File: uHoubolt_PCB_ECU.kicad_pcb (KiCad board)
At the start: 4 copper layers, 118 parts, among them J1 Power In, J10 Servo 1, J11 PYRO 1, J2 Conn_02x04_Odd_Even, J3 CAN1, J4 CAN2, J5 CAN1, J6 CAN2, J7 Pressure 1, J8 TEMP 1, J9 OUT 1, Q1 SISA88DN or similar, U1 SiC431CED-T1-GE3, U10 INA180A1, U11 INA180A1, U2 TS30041-M050QFNR, U3 MCP1700-3302E, U4 MCP2562FDT-H_SN, U5 MCP2562FDT-H_SN, U6 STM32G491MET6-LQFP80, U7 ICM-20602, U8 W25Q256JV, U9 TPS1HC100, X1 TXC-7C

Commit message: schematic even more done
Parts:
- removed C24: 100n, Capacitor_SMD:C_0402_1005Metric
- added JP2: VDD, Jumper:SolderJumper-2_P1.3mm_Bridged_RoundedPad1.0x1.5mm, F.Cu at (86.0, 124.0)
- added JP3: VDRV, Jumper:SolderJumper-2_P1.3mm_Bridged_RoundedPad1.0x1.5mm, F.Cu at (90.3, 124.0)
- C10: value 10µ -> 100µ; footprint Capacitor_SMD:C_0603_1608Metric -> Capacitor_SMD:C_1210_3225Metric
- C25: value 10n -> 100n
- C28, C29: value 1u -> 2µ2
- C3: value 4µ7 -> 22µ
- C30: value 1u -> 100n; footprint Capacitor_SMD:C_0603_1608Metric -> Capacitor_SMD:C_0402_1005Metric
- C4: value 1µ -> 2µ2
- J1: footprint Connector_Molex:Molex_Mega-Fit_76825-0004_2x02_P5.70mm_Horizontal -> TXV_LIB:Molex_MegaFit_1x03
- J11: footprint Connector_Molex:Molex_SL_171971-0002_1x02_P2.54mm_Vertical -> TXV_LIB:Molex_SL_1x2
- J2: value Conn_02x04_Odd_Even -> Debug
- LS1: value Speaker_Crystal -> Speaker
- R10: value 115k -> 100k
- R11, R14, R16, R24, R27, R34, R4, R8: value 10k -> 9k1
- R12: value 6.8k -> 22k
- R13: value 4.7k -> 9k1
- R15: value 2k -> 9k1
- R19, R20, R21, R23: value LED -> 120
- R28: value 1k -> 120
- R3, R6: value LED -> 1k
- R33, R36: value 10k -> 22k
- R5, R9: value 2k -> 1k
- U1: value SiC431CED-T1-GE3 -> SiC431C
- U10, U11: value INA180A1 -> INA180B1; footprint Package_TO_SOT_SMD:SOT-23-6 -> Package_TO_SOT_SMD:SOT-23-5
- U5: value MCP2562FDT-H_SN -> MCP2562FDT
- moved R12 89.6 mm to (85.0, 92.0)
- moved R13 77.7 mm to (86.0, 95.0)
- moved C21 25.6 mm to (166.5, 121.2)
- moved C22 25.6 mm to (165.4, 123.4)
- moved C26 25.6 mm to (166.7, 118.2)
- moved C27 25.6 mm to (167.9, 124.5)
- moved R17 25.6 mm to (170.1, 121.0)
- moved R18 25.6 mm to (172.2, 124.2)
- moved J6 21.5 mm to (154.7, 113.5)
- moved C30 16.5 mm to (144.0, 38.0)
- moved U5 14.2 mm to (154.7, 125.3), turned to 90 degrees
- moved U4 14.1 mm to (145.3, 125.3), turned to 90 degrees
- moved J1 13.4 mm to (67.5, 61.0), turned to 90 degrees
- moved R22 13.0 mm to (207.7, 90.5)
- moved J3 12.6 mm to (145.3, 119.9)
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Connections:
- net /Buzzer_N renamed /Speaker_N
- net /Buzzer_P renamed /Speaker_P
- C1 pad 1: Net-(C1-Pad1) -> +12V
- C2 pad 1: Net-(C1-Pad1) -> +12V
- C5 pad 1: Net-(C1-Pad1) -> +12V
- C6 pad 1: Net-(C1-Pad1) -> +12V
- C7 pad 1: Net-(C1-Pad1) -> +12V
- J8 pad MP: (no net) -> GND
- U1 pad 1: Net-(C1-Pad1) -> +12V
- U1 pad 2: Net-(C1-Pad1) -> +12V
- U1 pad 22: Net-(C1-Pad1) -> +12V
- U1 pad 26: Net-(C1-Pad1) -> +12V
- U10 pad 1: Net-(R25-Pad2) -> Net-(J7-Pad2)
- U10 pad 3: Net-(J7-Pad2) -> Net-(J7-Pad3)
- U10 pad 4: Net-(J7-Pad3) -> Net-(R25-Pad2)
- U10 pad 5: (no net) -> +3V3
- U11 pad 1: /SERVO_1_CURR -> +7.4V
- U11 pad 3: +7.4V -> Net-(J10-Pad3)
- U11 pad 4: Net-(J10-Pad3) -> /SERVO_1_CURR
- U11 pad 5: (no net) -> +3V3
- U5 pad 9: (no net) -> GND
- U6 pad 59: Net-(U6-Pad59) -> /CAN1_RX
- U6 pad 60: Net-(U6-Pad60) -> /CAN1_TX
- U6 pad 65: Net-(U6-Pad65) -> /SPI_IMU_CS
- U6 pad 66: Net-(U6-Pad66) -> /SPI_SCK
- U6 pad 67: Net-(U6-Pad67) -> /SPI_MISO
- U6 pad 68: Net-(U6-Pad68) -> /SPI_MOSI
- U6 pad 69: Net-(U6-Pad69) -> /IMU_INT
- U6 pad 74: Net-(U6-Pad74) -> /CAN2_RX
- U6 pad 75: Net-(U6-Pad75) -> /CAN2_TX
- U7 pad 2: /SPI_CLK -> /SPI_SCK
- U7 pad 6: /IMU_INTERRUPT -> /IMU_INT
- U9 pad 8: Net-(U9-Pad8) -> Net-(J11-Pad1)
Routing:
- net /PRESS_1: track 4.20 -> 1.43 mm
- net Net-(R25-Pad2): track 2.90 -> 4.88 mm
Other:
- board outline added: 65 x 62 mm

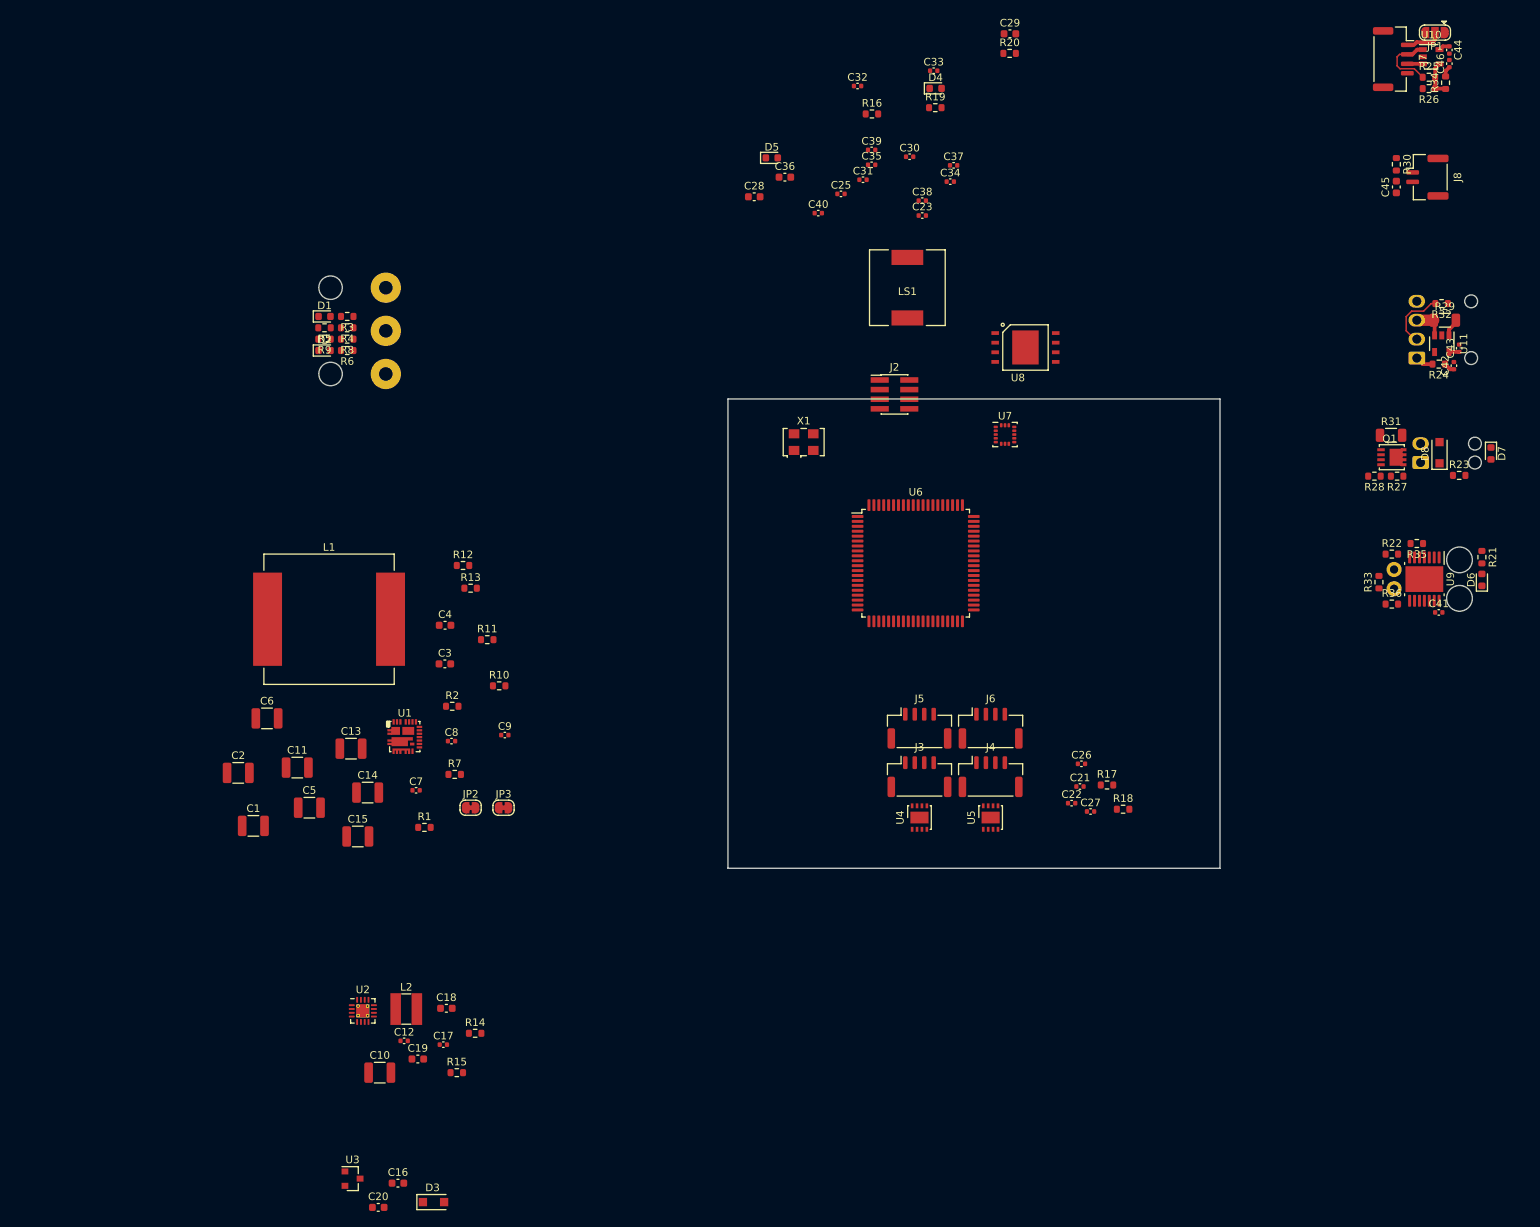
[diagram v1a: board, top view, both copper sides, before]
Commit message: moved I/O to subsheets, started layout
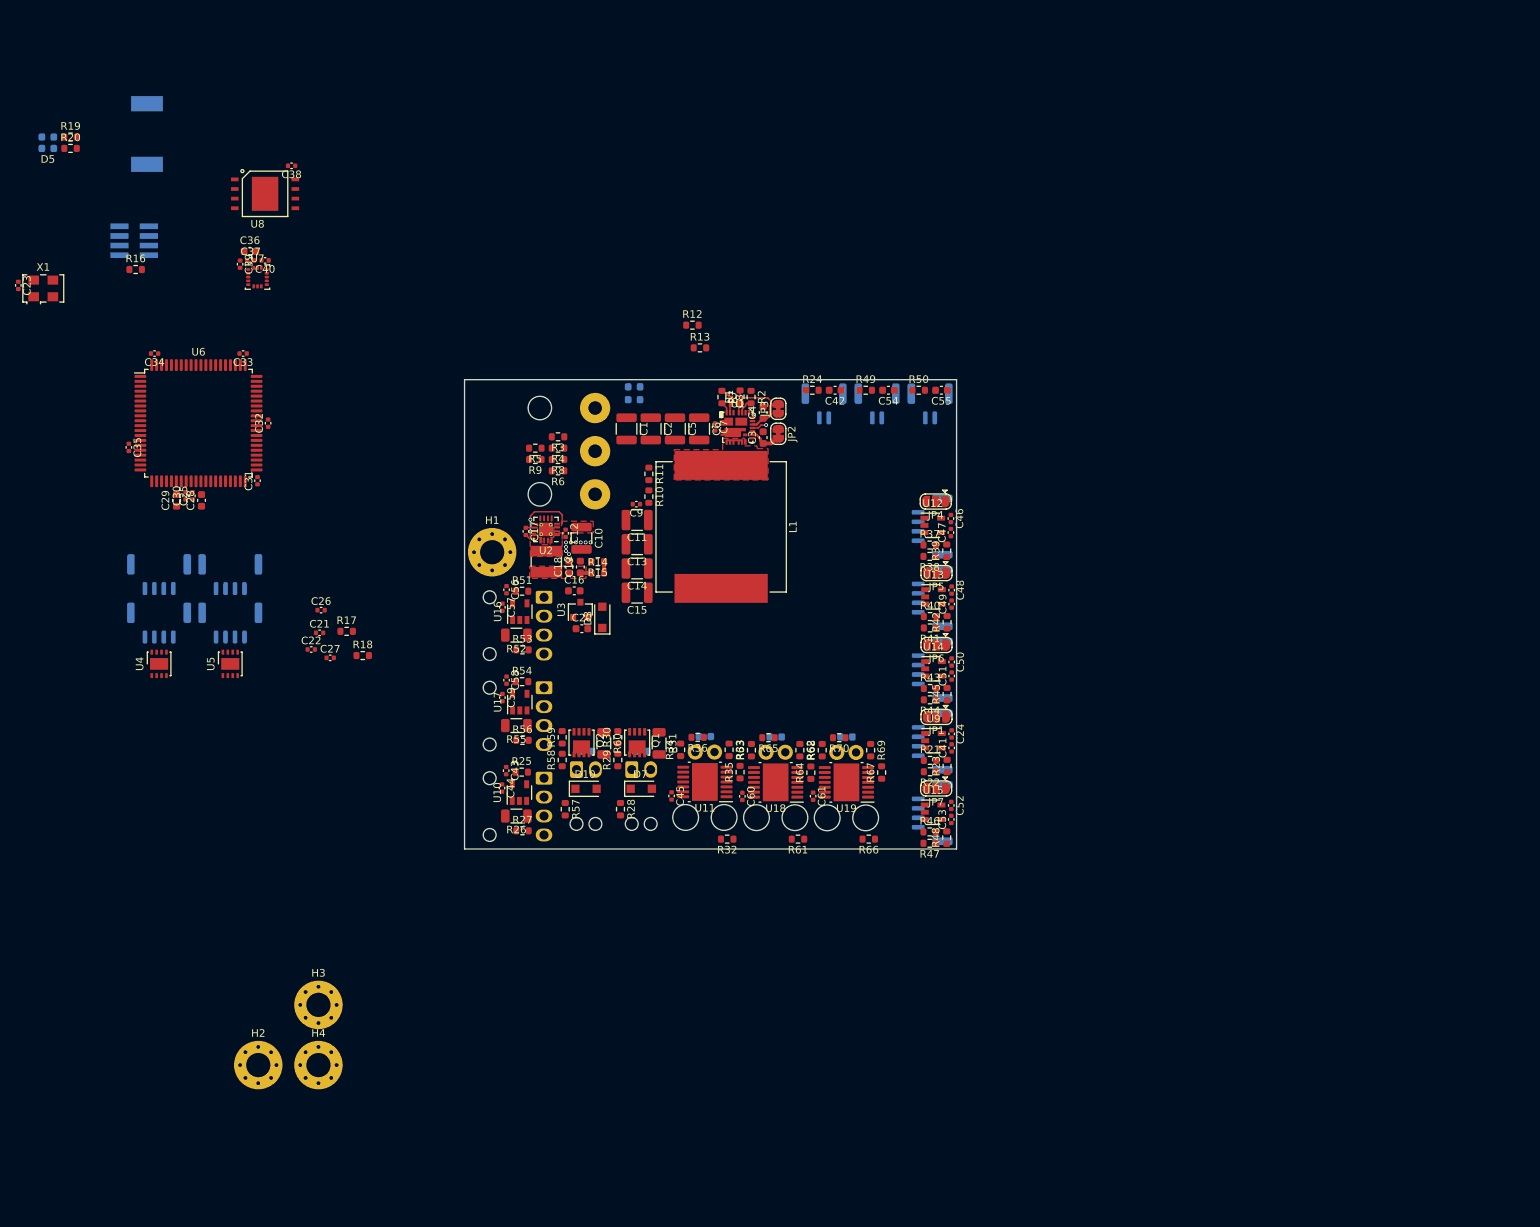
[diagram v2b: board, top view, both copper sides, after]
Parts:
- added C24: 100n, Capacitor_SMD:C_0402_1005Metric, F.Cu at (149.6, 114.2)
- added C47: 100n, Capacitor_SMD:C_0402_1005Metric, F.Cu at (149.4, 87.7)
- added C48: 100n, Capacitor_SMD:C_0402_1005Metric, F.Cu at (149.6, 95.2)
- added C49: 100n, Capacitor_SMD:C_0402_1005Metric, F.Cu at (149.6, 97.1)
- added C50: 100n, Capacitor_SMD:C_0402_1005Metric, F.Cu at (149.6, 104.8)
- added C51: 100n, Capacitor_SMD:C_0402_1005Metric, F.Cu at (149.6, 106.6)
- added C52: 100n, Capacitor_SMD:C_0402_1005Metric, F.Cu at (149.5, 123.7)
- added C53: 100n, Capacitor_SMD:C_0402_1005Metric, F.Cu at (149.5, 125.5)
- added C54: 22µ, Capacitor_SMD:C_0603_1608Metric, F.Cu at (141.2, 68.8)
- added C55: 22µ, Capacitor_SMD:C_0603_1608Metric, F.Cu at (148.2, 68.8)
- added C56: 100n, Capacitor_SMD:C_0402_1005Metric, F.Cu at (90.8, 95.2)
- added C57: 100n, Capacitor_SMD:C_0402_1005Metric, F.Cu at (90.2, 97.5)
- added C58: 100n, Capacitor_SMD:C_0402_1005Metric, F.Cu at (90.8, 107.2)
- added C59: 100n, Capacitor_SMD:C_0402_1005Metric, F.Cu at (90.2, 109.5)
- added C60: 100n, Capacitor_SMD:C_0402_1005Metric, F.Cu at (121.9, 122.5)
- added C61: 100n, Capacitor_SMD:C_0402_1005Metric, F.Cu at (131.2, 122.5)
- added D10: Shottky, Diode_SMD:D_SOD-123F, F.Cu at (101.2, 121.5)
- added D11: PYRO 1, LED_SMD:LED_0603_1608Metric, B.Cu at (126.3, 114.7)
- added D12: PYRO 1, LED_SMD:LED_0603_1608Metric, B.Cu at (135.7, 114.7)
- added D9: OUT 1, LED_SMD:LED_0603_1608Metric, B.Cu at (101.2, 116.5)
- added H1: MH, MountingHole:MountingHole_3.2mm_M3_Pad_Via, F.Cu at (88.8, 90.2)
- added H2: MH, MountingHole:MountingHole_3.2mm_M3_Pad_Via, F.Cu at (58.0, 158.0)
- added H3: MH, MountingHole:MountingHole_3.2mm_M3_Pad_Via, F.Cu at (65.9, 150.1)
- added H4: MH, MountingHole:MountingHole_3.2mm_M3_Pad_Via, F.Cu at (65.9, 158.0)
- added J12: Pressure 1, Connector_JST:JST_GH_SM04B-GHS-TB_1x04-1MP_P1.25mm_Horizontal, B.Cu at (147.0, 86.9)
- added J13: Pressure 1, Connector_JST:JST_GH_SM04B-GHS-TB_1x04-1MP_P1.25mm_Horizontal, B.Cu at (147.0, 96.3)
- added J14: Pressure 1, Connector_JST:JST_GH_SM04B-GHS-TB_1x04-1MP_P1.25mm_Horizontal, B.Cu at (147.0, 105.8)
- added J15: Pressure 1, Connector_JST:JST_GH_SM04B-GHS-TB_1x04-1MP_P1.25mm_Horizontal, B.Cu at (147.0, 124.7)
- added J16: TEMP 1, Connector_JST:JST_GH_SM02B-GHS-TB_1x02-1MP_P1.25mm_Horizontal, B.Cu at (139.7, 70.7)
- added J17: TEMP 1, Connector_JST:JST_GH_SM02B-GHS-TB_1x02-1MP_P1.25mm_Horizontal, B.Cu at (146.7, 70.7)
- added J18: Servo 1, Connector_Molex:Molex_Nano-Fit_105313-xx04_1x04_P2.50mm_Horizontal, B.Cu at (95.7, 96.2)
- added J19: Servo 1, Connector_Molex:Molex_Nano-Fit_105313-xx04_1x04_P2.50mm_Horizontal, B.Cu at (95.7, 108.2)
- added J20: OUT 1, Connector_Molex:Molex_Nano-Fit_105313-xx02_1x02_P2.50mm_Horizontal, B.Cu at (100.0, 119.0)
- added J21: PYRO 1, TXV_LIB:Molex_SL_1x2, B.Cu at (126.3, 116.7)
- added J22: PYRO 1, TXV_LIB:Molex_SL_1x2, B.Cu at (135.7, 116.7)
- added JP4: V_SEL, Jumper:SolderJumper-3_P1.3mm_Open_RoundedPad1.0x1.5mm, F.Cu at (147.4, 83.5)
- added JP5: V_SEL, Jumper:SolderJumper-3_P1.3mm_Open_RoundedPad1.0x1.5mm, F.Cu at (147.6, 93.0)
- added JP6: V_SEL, Jumper:SolderJumper-3_P1.3mm_Open_RoundedPad1.0x1.5mm, F.Cu at (147.6, 102.5)
- added JP7: V_SEL, Jumper:SolderJumper-3_P1.3mm_Open_RoundedPad1.0x1.5mm, F.Cu at (147.5, 121.5)
- added Q2: SISA88DN or similar, TXV_LIB:PowerPAK_1212-8, F.Cu at (100.7, 115.1)
- added R37: 4k7/0, Resistor_SMD:R_0603_1608Metric, F.Cu at (146.7, 89.3)
- added R38: 6k8/160, Resistor_SMD:R_0603_1608Metric, F.Cu at (146.7, 90.8)
- added R39: 9k1, Resistor_SMD:R_0603_1608Metric, F.Cu at (148.9, 90.0)
- added R40: 4k7/0, Resistor_SMD:R_0603_1608Metric, F.Cu at (146.7, 98.8)
- added R41: 6k8/160, Resistor_SMD:R_0603_1608Metric, F.Cu at (146.7, 100.2)
- added R42: 9k1, Resistor_SMD:R_0603_1608Metric, F.Cu at (148.9, 99.5)
- added R43: 4k7/0, Resistor_SMD:R_0603_1608Metric, F.Cu at (146.7, 108.2)
- added R44: 6k8/160, Resistor_SMD:R_0603_1608Metric, F.Cu at (146.7, 109.8)
- added R45: 9k1, Resistor_SMD:R_0603_1608Metric, F.Cu at (148.9, 109.0)
- added R46: 4k7/0, Resistor_SMD:R_0603_1608Metric, F.Cu at (146.7, 127.2)
- added R47: 6k8/160, Resistor_SMD:R_0603_1608Metric, F.Cu at (146.7, 128.7)
- added R48: 9k1, Resistor_SMD:R_0603_1608Metric, F.Cu at (148.9, 128.0)
- added R49: 1k, Resistor_SMD:R_0603_1608Metric, F.Cu at (138.2, 68.8)
- added R50: 1k, Resistor_SMD:R_0603_1608Metric, F.Cu at (145.2, 68.8)
- added R51: 9k1, Resistor_SMD:R_0603_1608Metric, F.Cu at (92.8, 95.4)
- added R52: 10m 1W, Resistor_SMD:R_1206_3216Metric, F.Cu at (92.0, 101.2)
- added R53: 1k, Resistor_SMD:R_0603_1608Metric, F.Cu at (92.8, 103.2)
- added R54: 9k1, Resistor_SMD:R_0603_1608Metric, F.Cu at (92.8, 107.3)
- added R55: 10m 1W, Resistor_SMD:R_1206_3216Metric, F.Cu at (92.0, 113.2)
- added R56: 1k, Resistor_SMD:R_0603_1608Metric, F.Cu at (92.8, 115.1)
- added R57: 120, Resistor_SMD:R_0603_1608Metric, F.Cu at (98.5, 124.2)
- added R58: 9k1, Resistor_SMD:R_0603_1608Metric, F.Cu at (98.1, 117.7)
- added R59: 120, Resistor_SMD:R_0603_1608Metric, F.Cu at (98.1, 114.7)
- added R60: 10m 1W, Resistor_SMD:R_1206_3216Metric, F.Cu at (103.6, 115.5)
- added R61: 120, Resistor_SMD:R_0603_1608Metric, F.Cu at (129.2, 128.2)
- added R62: 22k, Resistor_SMD:R_0603_1608Metric, F.Cu at (129.5, 116.4)
- added R63: 22k, Resistor_SMD:R_0603_1608Metric, F.Cu at (123.1, 116.4)
- added R64: 1k, Resistor_SMD:R_0603_1608Metric, F.Cu at (130.9, 119.4)
- added R65: 22k, Resistor_SMD:R_0603_1608Metric, F.Cu at (125.3, 114.8)
- added R66: 120, Resistor_SMD:R_0603_1608Metric, F.Cu at (138.6, 128.2)
- added R67: 22k, Resistor_SMD:R_0603_1608Metric, F.Cu at (140.3, 119.3)
- added R68: 22k, Resistor_SMD:R_0603_1608Metric, F.Cu at (132.4, 116.4)
- added R69: 1k, Resistor_SMD:R_0603_1608Metric, F.Cu at (138.8, 116.4)
- added R70: 22k, Resistor_SMD:R_0603_1608Metric, F.Cu at (134.7, 114.8)
- added U12: INA180B1, Package_TO_SOT_SMD:SOT-23-5, F.Cu at (147.1, 86.7)
- added U13: INA180B1, Package_TO_SOT_SMD:SOT-23-5, F.Cu at (147.2, 96.2)
- added U14: INA180B1, Package_TO_SOT_SMD:SOT-23-5, F.Cu at (147.2, 105.7)
- added U15: INA180B1, Package_TO_SOT_SMD:SOT-23-5, F.Cu at (147.1, 124.6)
- added U16: INA180B1, Package_TO_SOT_SMD:SOT-23-5, F.Cu at (92.5, 98.1)
- added U17: INA180B1, Package_TO_SOT_SMD:SOT-23-5, F.Cu at (92.5, 110.0)
- added U18: TPS1HC100, Package_SO:HTSSOP-14-1EP_4.4x5mm_P0.65mm_EP3.4x5mm_Mask3x3.1mm, F.Cu at (126.3, 120.7)
- added U19: TPS1HC100, Package_SO:HTSSOP-14-1EP_4.4x5mm_P0.65mm_EP3.4x5mm_Mask3x3.1mm, F.Cu at (135.7, 120.7)
- C42: value 100n -> 22µ; footprint Capacitor_SMD:C_0402_1005Metric -> Capacitor_SMD:C_0603_1608Metric
- C45: value 22µ -> 100n; footprint Capacitor_SMD:C_0603_1608Metric -> Capacitor_SMD:C_0402_1005Metric
- D1, D2, D4, D5, J2, J3, J4, J5, J6, J7, LS1: moved to B.Cu
- D6: value PYRO 1 -> OUT 1; moved to B.Cu
- D7: value OUT 1 -> Shottky; footprint LED_SMD:LED_0603_1608Metric -> Diode_SMD:D_SOD-123F
- D8: value Shottky -> PYRO 1; footprint Diode_SMD:D_SOD-123F -> LED_SMD:LED_0603_1608Metric; moved to B.Cu
- J10: value Servo 1 -> OUT 1; footprint Connector_Molex:Molex_Nano-Fit_105313-xx04_1x04_P2.50mm_Horizontal -> Connector_Molex:Molex_Nano-Fit_105313-xx02_1x02_P2.50mm_Horizontal
- J8: footprint Connector_JST:JST_GH_BM02B-GHS-TBT_1x02-1MP_P1.25mm_Vertical -> Connector_JST:JST_GH_SM02B-GHS-TB_1x02-1MP_P1.25mm_Horizontal; moved to B.Cu
- J9: value OUT 1 -> Servo 1; footprint Connector_Molex:Molex_Nano-Fit_105313-xx02_1x02_P2.50mm_Horizontal -> Connector_Molex:Molex_Nano-Fit_105313-xx04_1x04_P2.50mm_Horizontal
- R21: value 120 -> 4k7/0
- R22: value 22k -> 6k8/160
- R23: value 120 -> 9k1
- R24, R27: value 9k1 -> 1k
- R25: value 4k7/0 -> 9k1
- R26: value 6k8/160 -> 10m 1W; footprint Resistor_SMD:R_0603_1608Metric -> Resistor_SMD:R_1206_3216Metric
- R29: value 10m 1W -> 9k1; footprint Resistor_SMD:R_1206_3216Metric -> Resistor_SMD:R_0603_1608Metric
- R30, R32: value 1k -> 120
- R34: value 9k1 -> 22k
- U11: value INA180B1 -> TPS1HC100; footprint Package_TO_SOT_SMD:SOT-23-5 -> Package_SO:HTSSOP-14-1EP_4.4x5mm_P0.65mm_EP3.4x5mm_Mask3x3.1mm
- U9: value TPS1HC100 -> INA180B1; footprint Package_SO:HTSSOP-14-1EP_4.4x5mm_P0.65mm_EP3.4x5mm_Mask3x3.1mm -> Package_TO_SOT_SMD:SOT-23-5
- moved C44 158.6 mm to (90.2, 121.4)
- moved U10 154.8 mm to (92.5, 122.0), turned to 90 degrees
- moved R26 154.2 mm to (92.0, 125.1)
- moved R25 151.0 mm to (92.8, 119.3)
- moved C43 137.7 mm to (90.7, 119.1), turned to 270 degrees
- moved R34 134.1 mm to (113.8, 116.3)
- moved R30 127.7 mm to (105.5, 114.7), turned to 90 degrees
- moved C29 126.2 mm to (47.1, 83.4), turned to 90 degrees
- moved C45 125.1 mm to (112.5, 122.5), turned to 270 degrees
- moved R20 124.7 mm to (33.1, 36.9)
- moved R27 124.7 mm to (92.8, 127.0), turned to 0 degrees
- moved R29 123.7 mm to (105.5, 117.7), turned to 90 degrees
- moved J9 123.1 mm to (95.7, 120.1), turned to 180 degrees
- moved D7 120.7 mm to (108.5, 121.5), turned to 0 degrees
- moved C23 119.8 mm to (26.2, 55.0), turned to 270 degrees
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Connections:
- net /OUT_1_CURR renamed /OUT_2_CURR
- C41 pad 1: PYRO -> /PRESS_1
- C42 pad 1: /SERVO_1_FDBK -> GND
- C42 pad 2: GND -> /TEMP_1
- C43 pad 1: +3V3 -> /SERVO_1_FDBK
- C45 pad 1: GND -> PYRO
- C45 pad 2: /TEMP_1 -> GND
- C46 pad 1: /PRESS_1 -> +3V3
- D7 pad 1: GND -> +12V
- D8 pad 1: +12V -> GND
- J10 pad 1: Net-(J10-Pad1) -> +12V
- J10 pad 2: Net-(J10-Pad2) -> Net-(D7-Pad2)
- J9 pad 1: +12V -> Net-(J9-Pad1)
- J9 pad 2: Net-(D8-Pad2) -> Net-(J9-Pad2)
- Q1 pad 2: Net-(D8-Pad2) -> Net-(D7-Pad2)
- R21 pad 1: /PYRO_1_CTRL -> Net-(J7-Pad2)
- R21 pad 2: Net-(D6-Pad2) -> Net-(R21-Pad2)
- R22 pad 1: GND -> Net-(R21-Pad2)
- R22 pad 2: Net-(R22-Pad2) -> GND
- R23 pad 1: /OUT_1_CTRL -> Net-(R21-Pad2)
- R23 pad 2: Net-(D7-Pad2) -> /PRESS_1
- R24 pad 1: /SERVO_1_FDBK -> +3V3
- R24 pad 2: Net-(J10-Pad1) -> /TEMP_1
- R25 pad 1: Net-(J7-Pad2) -> /SERVO_1_FDBK
- R25 pad 2: Net-(R25-Pad2) -> Net-(J9-Pad1)
- R26 pad 1: Net-(R25-Pad2) -> Net-(J9-Pad3)
- R26 pad 2: GND -> +7.4V
- R27 pad 1: GND -> /SERVO_1_PWM
- R27 pad 2: /OUT_1_CTRL -> Net-(J9-Pad2)
- R28 pad 2: Net-(Q1-Pad1) -> Net-(D6-Pad2)
- R29 pad 1: Net-(J10-Pad3) -> GND
- R29 pad 2: +7.4V -> /OUT_1_CTRL
- R30 pad 1: +3V3 -> /OUT_1_CTRL
- R30 pad 2: /TEMP_1 -> Net-(Q1-Pad1)
- R32 pad 1: /SERVO_1_PWM -> /PYRO_1_CTRL
- R32 pad 2: Net-(J10-Pad2) -> Net-(D8-Pad2)
- R33 pad 1: Net-(J11-Pad1) -> GND
- R33 pad 2: +3V3 -> Net-(R33-Pad2)
- R34 pad 1: Net-(R25-Pad2) -> Net-(J11-Pad1)
- R34 pad 2: /PRESS_1 -> +3V3
- U10 pad 1: Net-(J7-Pad2) -> +7.4V
- U10 pad 3: Net-(J7-Pad3) -> Net-(J9-Pad3)
- U10 pad 4: Net-(R25-Pad2) -> /SERVO_1_CURR
- U11 pad 1: +7.4V -> GND
- U11 pad 2: GND -> /PYRO_1_CTRL
- U11 pad 3: Net-(J10-Pad3) -> +3V3
- U11 pad 4: /SERVO_1_CURR -> Net-(U11-Pad4)
- U11 pad 5: +3V3 -> GND
- U9 pad 1: GND -> Net-(J7-Pad2)
- U9 pad 2: /PYRO_1_CTRL -> GND
- U9 pad 3: +3V3 -> Net-(J7-Pad3)
- U9 pad 4: Net-(U9-Pad4) -> Net-(R21-Pad2)
- U9 pad 5: GND -> +3V3
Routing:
- net Net-(C4-Pad1): track 0.00 -> 10.8 mm
- net Net-(J7-Pad2): track 9.15 -> 0.00 mm
- net +12V: track 0.00 -> 8.45 mm, vias 0 -> 2
- net Net-(J10-Pad2): track 8.30 -> 0.00 mm
- net Net-(R25-Pad2): track 4.88 -> 0.00 mm
- net Net-(J7-Pad1): track 4.88 -> 0.00 mm
- net Net-(C3-Pad1): track 0.00 -> 4.31 mm
- net Net-(J10-Pad3): track 4.28 -> 0.00 mm
- net +3V3: track 2.84 -> 0.00 mm
- net Net-(J10-Pad1): track 2.41 -> 0.00 mm
- net Net-(J7-Pad3): track 2.31 -> 0.00 mm
- net Net-(R2-Pad2): track 0.00 -> 2.06 mm
- net /7V4_PGOOD: track 0.00 -> 1.97 mm, vias 0 -> 1
- net Net-(C8-Pad1): track 0.00 -> 1.70 mm
- net +7.4V: track 2.38 -> 0.73 mm, vias 0 -> 1
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- added copper zone on F.Cu, net +12V
- added copper zone on F.Cu, net +5V
- added copper zone on F.Cu, net Net-(C17-Pad2)
- added copper zone on F.Cu, net Net-(L1-Pad1)
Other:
- net class Default: clearance 0.2 -> 0.15; via_dia 0.8 -> 0.5; via_drill 0.4 -> 0.3
- rule trace_clearance: 0.2 -> 0.15

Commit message: preliminary placement done
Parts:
- C1, C11, C13, C14, C15, C2, C3, C4, C5, C6, C7, C8, C9, JP2, JP3, L1, R1, R10, R11, R2, R7, U1: moved to B.Cu
- J10, J20: footprint Connector_Molex:Molex_Nano-Fit_105313-xx02_1x02_P2.50mm_Horizontal -> TXV_LIB:Molex_Nano-Fit_105313-xx02_1x02_P2.50mm_Horizontal
- J12, J13, J14, J15, J3, J4, J5, J6, J7: footprint Connector_JST:JST_GH_SM04B-GHS-TB_1x04-1MP_P1.25mm_Horizontal -> Connector_JST:JST_GH_BM04B-GHS-TBT_1x04-1MP_P1.25mm_Vertical
- J16, J17, J8: footprint Connector_JST:JST_GH_SM02B-GHS-TB_1x02-1MP_P1.25mm_Horizontal -> Connector_JST:JST_GH_BM02B-GHS-TBT_1x02-1MP_P1.25mm_Vertical
- J18, J19, J9: footprint Connector_Molex:Molex_Nano-Fit_105313-xx04_1x04_P2.50mm_Horizontal -> TXV_LIB:Molex_Nano-Fit_105313-xx04_1x04_P2.50mm_Horizontal
- LS1: moved to F.Cu
- moved D4 174.1 mm to (177.9, 127.5), turned to 270 degrees
- moved R19 173.2 mm to (177.9, 130.5), turned to 270 degrees
- moved D5 172.0 mm to (176.4, 127.5), turned to 270 degrees
- moved R20 171.1 mm to (176.4, 130.5), turned to 270 degrees
- moved LS1 156.5 mm to (165.1, 133.3), turned to 270 degrees
- moved C23 142.3 mm to (162.6, 95.9), turned to 90 degrees
- moved X1 135.8 mm to (159.2, 95.5), turned to 180 degrees
- moved J2 131.1 mm to (167.9, 84.2), turned to 180 degrees
- moved C36 130.6 mm to (169.1, 117.4), turned to 270 degrees
- moved J3 129.2 mm to (169.1, 135.2), turned to 90 degrees
- moved C37 129.0 mm to (167.8, 117.5), turned to 270 degrees
- moved C39 128.8 mm to (167.3, 116.1), turned to 180 degrees
- moved H3 128.4 mm to (176.0, 84.0)
- moved C40 128.3 mm to (167.8, 119.4), turned to 90 degrees
- moved U7 125.6 mm to (165.7, 118.4), turned to 270 degrees
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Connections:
- U4 pad 9: (no net) -> GND
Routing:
- added copper zone on B.Cu, net GND
- added copper zone on F.Cu, net GND
- added copper zone on B.Cu, net Net-(L1-Pad1)
- removed copper zone on F.Cu, net Net-(L1-Pad1)
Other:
- board size 65 x 62 mm -> 60 x 60 mm

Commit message: small changes, added Step File
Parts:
- moved C10 0.61 mm to (126.5, 117.6)
- moved C18 0.61 mm to (122.7, 116.0)
- moved C19 0.61 mm to (122.7, 117.5)
- moved U2 0.61 mm to (127.6, 112.9)
- moved C12 0.61 mm to (127.1, 115.5)
- moved C17 0.61 mm to (127.3, 110.2)
- moved L2 0.61 mm to (123.3, 113.0)
- moved R14 0.61 mm to (121.8, 119.8)
- moved R15 0.61 mm to (123.3, 119.8)
- moved D1 0.20 mm to (121.9, 126.2)
- moved D2 0.20 mm to (126.3, 126.2)
- moved R3 0.20 mm to (121.8, 123.2)
- moved R4 0.20 mm to (123.3, 123.2)
- moved R5 0.20 mm to (123.3, 126.2)
- moved R6 0.20 mm to (126.3, 123.2)
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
